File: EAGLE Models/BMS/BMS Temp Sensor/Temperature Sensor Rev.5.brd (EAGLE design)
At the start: 16.6 x 19.5 mm, 7 parts

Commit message: Set Resistance Values for the Temp Sense Board and Fixed ADC Connections
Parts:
- renumbered U$1 to IC1
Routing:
- net VCC: track 0.00 -> 13.9 mm
- net OUTPUT: track 0.00 -> 4.00 mm
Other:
- board size 16.6 x 19.5 mm -> 15.4 x 19.5 mm
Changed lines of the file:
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@@
 <board>
 <plain>
-<wire x1="0" y1="0" x2="16.635" y2="0" width="0" layer="20"/>
-<wire x1="16.635" y1="0" x2="16.635" y2="19.49" width="0" layer="20"/>
-<wire x1="16.635" y1="19.49" x2="0" y2="19.46" width="0" layer="20"/>
+<wire x1="0" y1="0" x2="15.365" y2="0" width="0" layer="20"/>
+<wire x1="15.365" y1="0" x2="15.365" y2="19.49" width="0" layer="20"/>
+<wire x1="15.365" y1="19.49" x2="0" y2="19.46" width="0" layer="20"/>
 <wire x1="0" y1="19.46" x2="0" y2="0" width="0" layer="20"/>
 <hole x="2.54" y="1.27" drill="0.6"/>
@@
 <element name="VCC_IN" library="wirepad" package="1,6/0,8" value="" x="7.62" y="13.335"/>
 <element name="VCC_OUT" library="wirepad" package="1,6/0,8" value="" x="7.62" y="3.81"/>
-<element name="U$1" library="microchip" package="SOT23" value="MCP970X" x="10.16" y="8.255"/>
+<element name="IC1" library="microchip" package="SOT23" value="MCP970X" x="10.16" y="8.255"/>
 <element name="C1" library="adafruit" package="C0603" value="" x="5.08" y="7.62"/>
 </elements>
@@
 <contactref element="VCC_IN" pad="1"/>
 <contactref element="VCC_OUT" pad="1"/>
-<contactref element="U$1" pad="1"/>
+<contactref element="IC1" pad="1"/>
 <contactref element="C1" pad="2"/>
-<wire x1="5.93" y1="7.62" x2="7.62" y2="13.335" width="0" layer="19" extent="1-1"/>
-<wire x1="9.21" y1="7.155" x2="5.93" y2="7.62" width="0" layer="19" extent="1-1"/>
-<wire x1="7.62" y1="3.81" x2="9.21" y2="7.155" width="0" layer="19" extent="1-1"/>
+<wire x1="7.62" y1="3.81" x2="7.62" y2="5.565" width="0.4064" layer="1"/>
+<wire x1="7.62" y1="5.565" x2="9.21" y2="7.155" width="0.4064" layer="1"/>
+<wire x1="9.21" y1="7.155" x2="6.395" y2="7.155" width="0.4064" layer="1"/>
+<wire x1="6.395" y1="7.155" x2="5.93" y2="7.62" width="0.4064" layer="1"/>
+<wire x1="5.93" y1="7.62" x2="5.93" y2="11.645" width="0.4064" layer="1"/>
+<wire x1="5.93" y1="11.645" x2="7.62" y2="13.335" width="0.4064" layer="1"/>
 </signal>
 <signal name="GND">
@@
 <polygon width="0.4064" layer="1">
 <vertex x="0" y="0"/>
-<vertex x="16.635" y="0"/>
-<vertex x="16.635" y="19.46"/>
+<vertex x="15.365" y="0"/>
+<vertex x="15.365" y="19.46"/>
 <vertex x="0" y="19.46"/>
 </polygon>
 <polygon width="0.4064" layer="16">
 <vertex x="0" y="0"/>
-<vertex x="16.635" y="0"/>
-<vertex x="16.635" y="19.46"/>
+<vertex x="15.365" y="0"/>
+<vertex x="15.365" y="19.46"/>
 <vertex x="0" y="19.46"/>
 </polygon>
-<contactref element="U$1" pad="3"/>
+<contactref element="IC1" pad="3"/>
 <contactref element="C1" pad="1"/>
 </signal>
 <signal name="OUTPUT">
 <contactref element="OUTPUT" pad="1"/>
-<contactref element="U$1" pad="2"/>
-<wire x1="11.11" y1="7.155" x2="12.7" y2="3.81" width="0" layer="19" extent="1-1"/>
+<contactref element="IC1" pad="2"/>
+<wire x1="12.7" y1="3.81" x2="12.7" y2="5.565" width="0.4064" layer="1"/>
+<wire x1="12.7" y1="5.565" x2="11.11" y2="7.155" width="0.4064" layer="1"/>
 </signal>
 </signals>

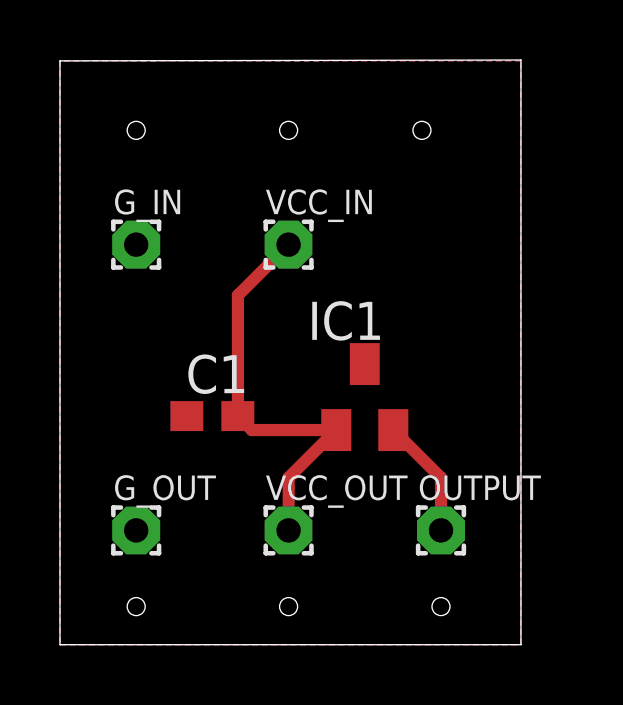
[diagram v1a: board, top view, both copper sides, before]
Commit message: Temp Sense Board Layouts Finished First revision, bunch of test layouts to get estimate of board sizes
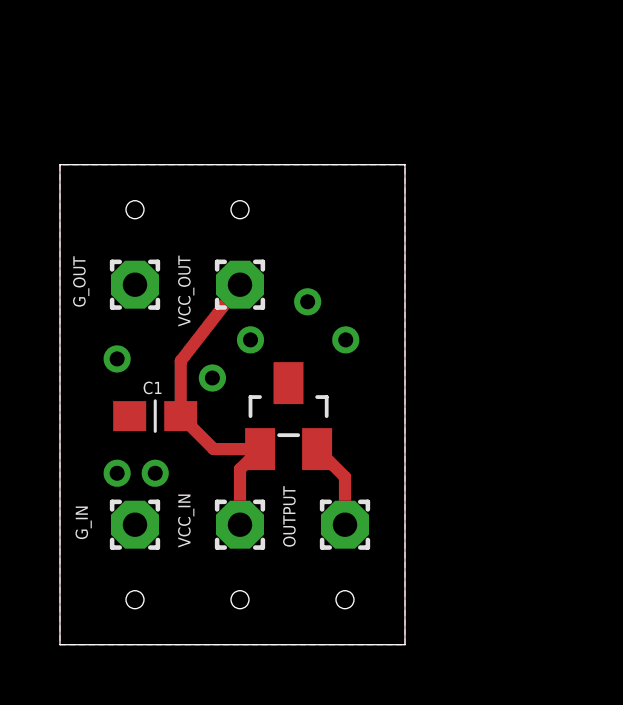
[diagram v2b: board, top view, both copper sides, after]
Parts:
- removed IC1: MCP970X, microchip:SOT23
- added U$1: MCP970X, microchip:SOT23
- moved VCC_IN 9.47 mm to (6.00, 4.00)
- moved G_IN 9.34 mm to (2.50, 4.00)
- moved VCC_OUT 8.35 mm to (6.00, 12.0)
- moved G_OUT 8.19 mm to (2.50, 12.0)
- moved OUTPUT 3.21 mm to (9.50, 4.00)
- moved C1 1.91 mm to (3.17, 7.62)
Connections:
- net GND: now also U$1.3; no longer IC1.3
- net OUTPUT: now also U$1.2; no longer IC1.2
- net VCC: now also U$1.1; no longer IC1.1
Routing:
- net VCC: track 13.9 -> 11.0 mm
- net OUTPUT: track 4.00 -> 2.91 mm
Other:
- board size 15.4 x 19.5 mm -> 11.5 x 16 mm
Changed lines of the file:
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@@
 <setting verticaltext="up"/>
 </settings>
-<grid distance="0.05" unitdist="inch" unit="mm" style="lines" multiple="1" display="no" altdistance="0.025" altunitdist="inch" altunit="inch"/>
+<grid distance="0.05" unitdist="inch" unit="mm" style="lines" multiple="1" display="no" altdistance="0.025" altunitdist="inch" altunit="mm"/>
 <layers>
 <layer number="1" name="Top" color="4" fill="1" visible="yes" active="yes"/>
@@
 <board>
 <plain>
-<wire x1="0" y1="0" x2="15.365" y2="0" width="0" layer="20"/>
-<wire x1="15.365" y1="0" x2="15.365" y2="19.49" width="0" layer="20"/>
-<wire x1="15.365" y1="19.49" x2="0" y2="19.46" width="0" layer="20"/>
-<wire x1="0" y1="19.46" x2="0" y2="0" width="0" layer="20"/>
-<hole x="2.54" y="1.27" drill="0.6"/>
-<hole x="7.62" y="1.27" drill="0.6"/>
-<hole x="12.7" y="1.27" drill="0.6"/>
-<hole x="12.065" y="17.145" drill="0.6"/>
-<hole x="7.62" y="17.145" drill="0.6"/>
-<hole x="2.54" y="17.145" drill="0.6"/>
+<wire x1="0" y1="0" x2="11.5" y2="0" width="0" layer="20"/>
+<wire x1="11.5" y1="0" x2="11.5" y2="16" width="0" layer="20"/>
+<wire x1="11.5" y1="16" x2="0" y2="16" width="0" layer="20"/>
+<wire x1="0" y1="16" x2="0" y2="0" width="0" layer="20"/>
+<hole x="2.5" y="1.5" drill="0.6"/>
+<hole x="6" y="1.5" drill="0.6"/>
+<hole x="9.5" y="1.5" drill="0.6"/>
+<hole x="6" y="14.5" drill="0.6"/>
+<hole x="2.5" y="14.5" drill="0.6"/>
 </plain>
 <attributes>
@@
 </autorouter>
 <elements>
-<element name="G_IN" library="wirepad" package="1,6/0,8" value="" x="2.54" y="13.335"/>
-<element name="G_OUT" library="wirepad" package="1,6/0,8" value="" x="2.54" y="3.81"/>
-<element name="OUTPUT" library="wirepad" package="1,6/0,8" value="" x="12.7" y="3.81"/>
-<element name="VCC_IN" library="wirepad" package="1,6/0,8" value="" x="7.62" y="13.335"/>
-<element name="VCC_OUT" library="wirepad" package="1,6/0,8" value="" x="7.62" y="3.81"/>
-<element name="IC1" library="microchip" package="SOT23" value="MCP970X" x="10.16" y="8.255"/>
-<element name="C1" library="adafruit" package="C0603" value="" x="5.08" y="7.62"/>
+<element name="G_IN" library="wirepad" package="1,6/0,8" value="" x="2.5" y="4" smashed="yes">
+<attribute name="NAME" x="0.929" y="3.493" size="0.4064" layer="25" ratio="10" rot="R90"/>
+<attribute name="VALUE" x="2.5" y="4.6" size="0.0254" layer="27"/>
+</element>
+<element name="G_OUT" library="wirepad" package="1,6/0,8" value="" x="2.5" y="12" smashed="yes">
+<attribute name="NAME" x="0.849" y="11.238" size="0.4064" layer="25" ratio="10" rot="R90"/>
+<attribute name="VALUE" x="2.5" y="12.6" size="0.0254" layer="27"/>
+</element>
+<element name="OUTPUT" library="wirepad" package="1,6/0,8" value="" x="9.5" y="4" smashed="yes">
+<attribute name="NAME" x="7.849" y="3.238" size="0.4064" layer="25" ratio="10" rot="R90"/>
+<attribute name="VALUE" x="9.5" y="4.6" size="0.0254" layer="27"/>
+</element>
+<element name="VCC_IN" library="wirepad" package="1,6/0,8" value="" x="6" y="4" smashed="yes">
+<attribute name="NAME" x="4.349" y="3.238" size="0.4064" layer="25" ratio="10" rot="R90"/>
+<attribute name="VALUE" x="6" y="4.6" size="0.0254" layer="27"/>
+</element>
+<element name="VCC_OUT" library="wirepad" package="1,6/0,8" value="" x="6" y="12" smashed="yes">
+<attribute name="NAME" x="4.349" y="10.603" size="0.4064" layer="25" ratio="10" rot="R90"/>
+<attribute name="VALUE" x="6" y="12.6" size="0.0254" layer="27"/>
+</element>
+<element name="C1" library="adafruit" package="C0603" value="" x="3.175" y="7.62" smashed="yes">
+<attribute name="NAME" x="3.429" y="8.763" size="0.4064" layer="25" rot="R180"/>
+<attribute name="VALUE" x="2.286" y="5.588" size="1.27" layer="27"/>
+</element>
+<element name="U$1" library="microchip" package="SOT23" value="MCP970X" x="7.62" y="7.62" smashed="yes">
+<attribute name="VALUE" x="10.16" y="5.715" size="0.4064" layer="27" rot="R90"/>
+</element>
 </elements>
 <signals>
@@
 <contactref element="VCC_IN" pad="1"/>
 <contactref element="VCC_OUT" pad="1"/>
-<contactref element="IC1" pad="1"/>
 <contactref element="C1" pad="2"/>
-<wire x1="7.62" y1="3.81" x2="7.62" y2="5.565" width="0.4064" layer="1"/>
-<wire x1="7.62" y1="5.565" x2="9.21" y2="7.155" width="0.4064" layer="1"/>
-<wire x1="9.21" y1="7.155" x2="6.395" y2="7.155" width="0.4064" layer="1"/>
-<wire x1="6.395" y1="7.155" x2="5.93" y2="7.62" width="0.4064" layer="1"/>
-<wire x1="5.93" y1="7.62" x2="5.93" y2="11.645" width="0.4064" layer="1"/>
-<wire x1="5.93" y1="11.645" x2="7.62" y2="13.335" width="0.4064" layer="1"/>
+<contactref element="U$1" pad="1"/>
+<wire x1="6" y1="4" x2="6" y2="5.85" width="0.4064" layer="1"/>
+<wire x1="6" y1="5.85" x2="6.67" y2="6.52" width="0.4064" layer="1"/>
+<wire x1="6.67" y1="6.52" x2="5.125" y2="6.52" width="0.4064" layer="1"/>
+<wire x1="5.125" y1="6.52" x2="4.025" y2="7.62" width="0.4064" layer="1"/>
+<wire x1="4.025" y1="7.62" x2="4.025" y2="9.455" width="0.4064" layer="1"/>
+<wire x1="4.025" y1="9.455" x2="6" y2="12" width="0.4064" layer="1"/>
 </signal>
 <signal name="GND">
 <contactref element="G_IN" pad="1"/>
 <contactref element="G_OUT" pad="1"/>
-<polygon width="0.4064" layer="1">
+<polygon width="0.4064" layer="1" isolate="0.4064">
 <vertex x="0" y="0"/>
-<vertex x="15.365" y="0"/>
-<vertex x="15.365" y="19.46"/>
-<vertex x="0" y="19.46"/>
+<vertex x="11.5" y="0"/>
+<vertex x="11.5" y="16"/>
+<vertex x="0" y="16"/>
 </polygon>
-<polygon width="0.4064" layer="16">
+<polygon width="0.4064" layer="16" isolate="0.4064">
 <vertex x="0" y="0"/>
-<vertex x="15.365" y="0"/>
-<vertex x="15.365" y="19.46"/>
-<vertex x="0" y="19.46"/>
+<vertex x="11.5" y="0"/>
+<vertex x="11.5" y="16"/>
+<vertex x="0" y="16"/>
 </polygon>
-<contactref element="IC1" pad="3"/>
 <contactref element="C1" pad="1"/>
+<contactref element="U$1" pad="3"/>
+<via x="1.905" y="9.525" extent="1-16" drill="0.5"/>
+<via x="1.905" y="5.715" extent="1-16" drill="0.5"/>
+<via x="3.175" y="5.715" extent="1-16" drill="0.5"/>
+<via x="5.08" y="8.89" extent="1-16" drill="0.5"/>
+<via x="6.35" y="10.16" extent="1-16" drill="0.5"/>
+<via x="8.255" y="11.43" extent="1-16" drill="0.5"/>
+<via x="9.525" y="10.16" extent="1-16" drill="0.5"/>
 </signal>
 <signal name="OUTPUT">
 <contactref element="OUTPUT" pad="1"/>
-<contactref element="IC1" pad="2"/>
-<wire x1="12.7" y1="3.81" x2="12.7" y2="5.565" width="0.4064" layer="1"/>
-<wire x1="12.7" y1="5.565" x2="11.11" y2="7.155" width="0.4064" layer="1"/>
+<contactref element="U$1" pad="2"/>
+<wire x1="9.5" y1="4" x2="9.5" y2="5.59" width="0.4064" layer="1"/>
+<wire x1="9.5" y1="5.59" x2="8.57" y2="6.52" width="0.4064" layer="1"/>
 </signal>
 </signals>
+<errors>
+</errors>
 </board>
 </drawing>
